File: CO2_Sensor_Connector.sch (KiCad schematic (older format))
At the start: 8 parts

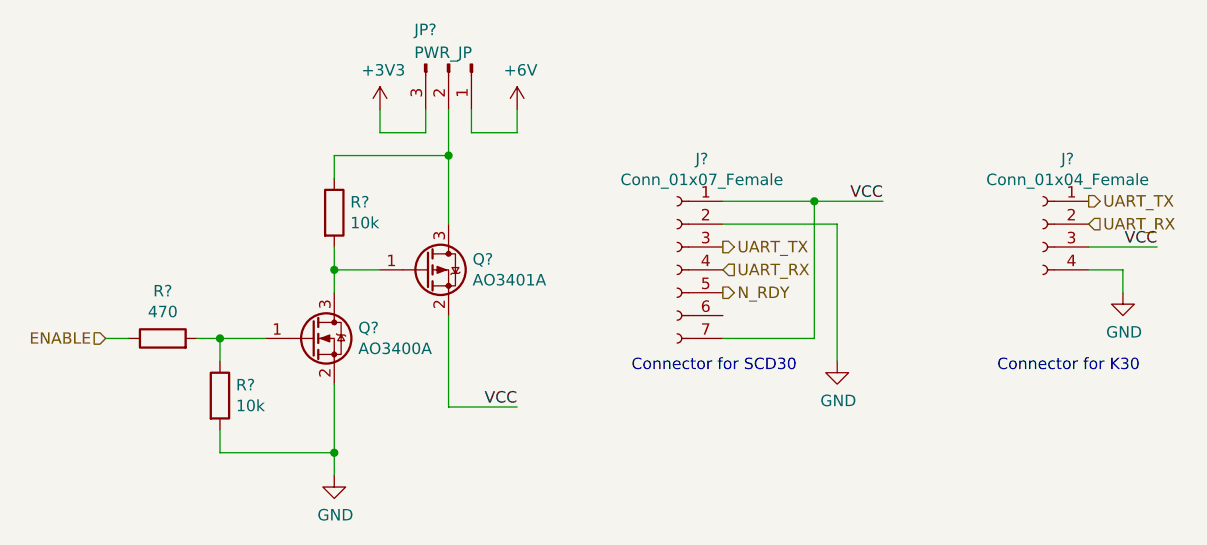
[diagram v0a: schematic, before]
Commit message: Change BME280 out for connector
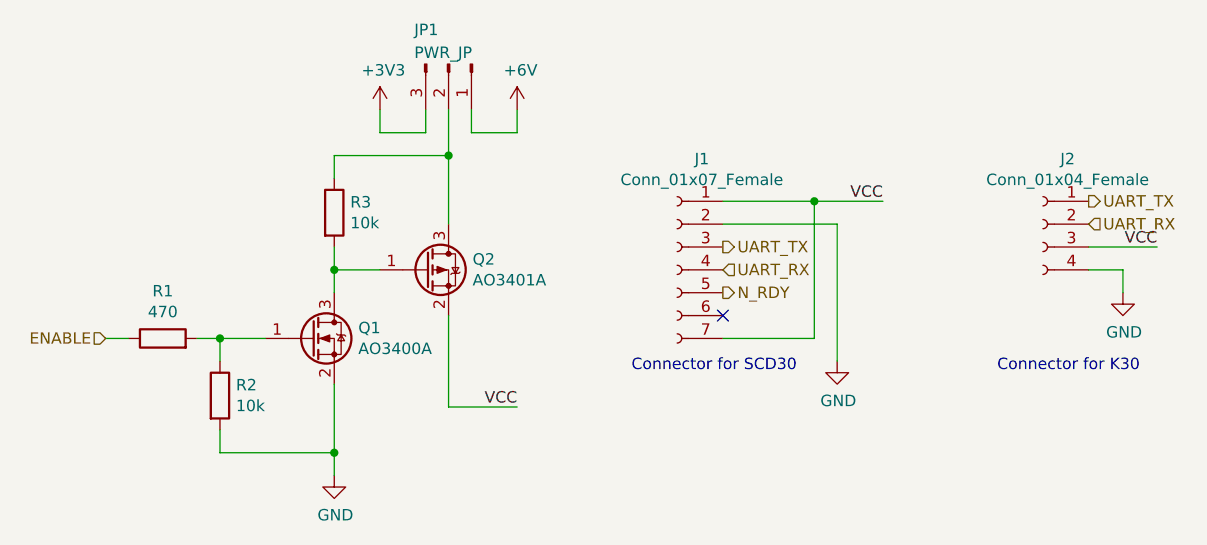
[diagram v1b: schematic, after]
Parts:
- gave numbers to parts that had none: 8
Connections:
- no-connect marks 0 -> 1
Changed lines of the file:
@@
 $Descr A4 11693 8268
 encoding utf-8
-Sheet 3 9
+Sheet 2 9
 Title ""
 Date ""
@@
 N_RDY
 $Comp
-L Connector:Conn_01x07_Female J?
+L Connector:Conn_01x07_Female J1
 U 1 1 60A57B40
 P 5800 3900
-AR Path="/60A49A7C/60A57B40" Ref="J?"  Part="1"
-AR Path="/60A4AC4A/60A57B40" Ref="J?"  Part="1"
-F 0 "J?" H 5692 4385 50  0000 C CNN
+AR Path="/60A49A7C/60A57B40" Ref="J1"  Part="1"
+AR Path="/60A4AC4A/60A57B40" Ref="J3"  Part="1"
+F 0 "J1" H 5692 4385 50  0000 C CNN
 F 1 "Conn_01x07_Female" H 5692 4294 50  0000 C CNN
 F 2 "" H 5800 3900 50  0001 C CNN
@@
 	6400 3600 6000 3600
 $Comp
-L power:GND #PWR?
+L power:GND #PWR04
 U 1 1 60A5D6A7
 P 6500 4300
-AR Path="/60A49A7C/60A5D6A7" Ref="#PWR?"  Part="1"
-AR Path="/60A4AC4A/60A5D6A7" Ref="#PWR?"  Part="1"
-F 0 "#PWR?" H 6500 4050 50  0001 C CNN
+AR Path="/60A49A7C/60A5D6A7" Ref="#PWR04"  Part="1"
+AR Path="/60A4AC4A/60A5D6A7" Ref="#PWR09"  Part="1"
+F 0 "#PWR09" H 6500 4050 50  0001 C CNN
 F 1 "GND" H 6505 4127 50  0000 C CNN
 F 2 "" H 6500 4300 50  0001 C CNN
@@
 	6400 4200 6400 3600
 $Comp
-L Transistor_FET:AO3401A Q?
+L Transistor_FET:AO3401A Q2
 U 1 1 60A6C14D
 P 4700 3900
-AR Path="/60A49A7C/60A6C14D" Ref="Q?"  Part="1"
-AR Path="/60A4AC4A/60A6C14D" Ref="Q?"  Part="1"
-F 0 "Q?" H 4905 3946 50  0000 L CNN
+AR Path="/60A49A7C/60A6C14D" Ref="Q2"  Part="1"
+AR Path="/60A4AC4A/60A6C14D" Ref="Q4"  Part="1"
+F 0 "Q2" H 4905 3946 50  0000 L CNN
 F 1 "AO3401A" H 4905 3855 50  0000 L CNN
 F 2 "Package_TO_SOT_SMD:SOT-23" H 4900 3825 50  0001 L CIN
@@
 $EndComp
 $Comp
-L Device:R R?
+L Device:R R1
 U 1 1 60A6FA21
 P 3550 4200
-AR Path="/60A49A7C/60A6FA21" Ref="R?"  Part="1"
-AR Path="/60A4AC4A/60A6FA21" Ref="R?"  Part="1"
-F 0 "R?" V 3757 4200 50  0000 C CNN
+AR Path="/60A49A7C/60A6FA21" Ref="R1"  Part="1"
+AR Path="/60A4AC4A/60A6FA21" Ref="R4"  Part="1"
+F 0 "R1" V 3757 4200 50  0000 C CNN
 F 1 "470" V 3666 4200 50  0000 C CNN
 F 2 "" V 3480 4200 50  0001 C CNN
@@
 	3400 4200 3300 4200
 $Comp
-L Device:R R?
+L Device:R R3
 U 1 1 60A736D3
 P 4300 3650
-AR Path="/60A49A7C/60A736D3" Ref="R?"  Part="1"
-AR Path="/60A4AC4A/60A736D3" Ref="R?"  Part="1"
-F 0 "R?" H 4370 3696 50  0000 L CNN
+AR Path="/60A49A7C/60A736D3" Ref="R3"  Part="1"
+AR Path="/60A4AC4A/60A736D3" Ref="R6"  Part="1"
+F 0 "R3" H 4370 3696 50  0000 L CNN
 F 1 "10k" H 4370 3605 50  0000 L CNN
 F 2 "" V 4230 3650 50  0001 C CNN
@@
 	4300 3500 4300 3400
 $Comp
-L Connector:Conn_01x03_Male JP?
+L Connector:Conn_01x03_Male JP1
 U 1 1 60A91C0B
 P 4800 3000
-AR Path="/60A49A7C/60A91C0B" Ref="JP?"  Part="1"
-AR Path="/60A4AC4A/60A91C0B" Ref="JP?"  Part="1"
-F 0 "JP?" V 4650 2850 50  0000 L CNN
+AR Path="/60A49A7C/60A91C0B" Ref="JP1"  Part="1"
+AR Path="/60A4AC4A/60A91C0B" Ref="JP2"  Part="1"
+F 0 "JP1" V 4650 2850 50  0000 L CNN
 F 1 "PWR_JP" V 4750 2850 50  0000 L CNN
 F 2 "" H 4800 3000 50  0001 C CNN
@@
 	4700 3200 4700 3300
 $Comp
-L power:+3V3 #PWR?
+L power:+3V3 #PWR02
 U 1 1 60A94D4D
 P 4500 3200
-AR Path="/60A49A7C/60A94D4D" Ref="#PWR?"  Part="1"
-AR Path="/60A4AC4A/60A94D4D" Ref="#PWR?"  Part="1"
-F 0 "#PWR?" H 4500 3050 50  0001 C CNN
+AR Path="/60A49A7C/60A94D4D" Ref="#PWR02"  Part="1"
+AR Path="/60A4AC4A/60A94D4D" Ref="#PWR07"  Part="1"
+F 0 "#PWR07" H 4500 3050 50  0001 C CNN
 F 1 "+3V3" H 4515 3373 50  0000 C CNN
 F 2 "" H 4500 3200 50  0001 C CNN
@@
 $EndComp
 $Comp
-L power:+6V #PWR?
+L power:+6V #PWR08
 U 1 1 60A9539A
 P 5100 3200
-AR Path="/60A49A7C/60A9539A" Ref="#PWR?"  Part="1"
-AR Path="/60A4AC4A/60A9539A" Ref="#PWR?"  Part="1"
-F 0 "#PWR?" H 5100 3050 50  0001 C CNN
+AR Path="/60A49A7C/60A9539A" Ref="#PWR08"  Part="1"
+AR Path="/60A4AC4A/60A9539A" Ref="#PWR0101"  Part="1"
+F 0 "#PWR0101" H 5100 3050 50  0001 C CNN
 F 1 "+6V" H 5115 3373 50  0000 C CNN
 F 2 "" H 5100 3200 50  0001 C CNN
@@
 	4900 3300 5100 3300
 $Comp
-L power:GND #PWR?
+L power:GND #PWR01
 U 1 1 60A9EA13
 P 4300 4800
-AR Path="/60A49A7C/60A9EA13" Ref="#PWR?"  Part="1"
-AR Path="/60A4AC4A/60A9EA13" Ref="#PWR?"  Part="1"
-F 0 "#PWR?" H 4300 4550 50  0001 C CNN
+AR Path="/60A49A7C/60A9EA13" Ref="#PWR01"  Part="1"
+AR Path="/60A4AC4A/60A9EA13" Ref="#PWR06"  Part="1"
+F 0 "#PWR06" H 4300 4550 50  0001 C CNN
 F 1 "GND" H 4305 4627 50  0000 C CNN
 F 2 "" H 4300 4800 50  0001 C CNN
@@
 VCC
 $Comp
-L Device:R R?
+L Device:R R2
 U 1 1 60AA508F
 P 3800 4450
-AR Path="/60A49A7C/60AA508F" Ref="R?"  Part="1"
-AR Path="/60A4AC4A/60AA508F" Ref="R?"  Part="1"
-F 0 "R?" H 3870 4496 50  0000 L CNN
+AR Path="/60A49A7C/60AA508F" Ref="R2"  Part="1"
+AR Path="/60A4AC4A/60AA508F" Ref="R5"  Part="1"
+F 0 "R2" H 3870 4496 50  0000 L CNN
 F 1 "10k" H 3870 4405 50  0000 L CNN
 F 2 "" V 3730 4450 50  0001 C CNN
@@
 	7600 3900 7750 3900
 $Comp
-L power:GND #PWR?
+L power:GND #PWR05
 U 1 1 60ABDE86
 P 7750 4000
-AR Path="/60A49A7C/60ABDE86" Ref="#PWR?"  Part="1"
-AR Path="/60A4AC4A/60ABDE86" Ref="#PWR?"  Part="1"
-F 0 "#PWR?" H 7750 3750 50  0001 C CNN
+AR Path="/60A49A7C/60ABDE86" Ref="#PWR05"  Part="1"
+AR Path="/60A4AC4A/60ABDE86" Ref="#PWR010"  Part="1"
+F 0 "#PWR010" H 7750 3750 50  0001 C CNN
 F 1 "GND" H 7755 3827 50  0000 C CNN
 F 2 "" H 7750 4000 50  0001 C CNN
@@
 $EndComp
 $Comp
-L Connector:Conn_01x04_Female J?
+L Connector:Conn_01x04_Female J2
 U 1 1 60ABE2B1
 P 7400 3700
-AR Path="/60A49A7C/60ABE2B1" Ref="J?"  Part="1"
-AR Path="/60A4AC4A/60ABE2B1" Ref="J?"  Part="1"
-F 0 "J?" H 7292 3985 50  0000 C CNN
+AR Path="/60A49A7C/60ABE2B1" Ref="J2"  Part="1"
+AR Path="/60A4AC4A/60ABE2B1" Ref="J4"  Part="1"
+F 0 "J2" H 7292 3985 50  0000 C CNN
 F 1 "Conn_01x04_Female" H 7292 3894 50  0000 C CNN
 F 2 "" H 7400 3700 50  0001 C CNN
@@
 	4800 4500 5100 4500
 $Comp
-L Transistor_FET:AO3400A Q?
+L Transistor_FET:AO3400A Q1
 U 1 1 60B57C20
 P 4200 4200
-AR Path="/60A49A7C/60B57C20" Ref="Q?"  Part="1"
-AR Path="/60A4AC4A/60B57C20" Ref="Q?"  Part="1"
-F 0 "Q?" H 4405 4246 50  0000 L CNN
+AR Path="/60A49A7C/60B57C20" Ref="Q1"  Part="1"
+AR Path="/60A4AC4A/60B57C20" Ref="Q3"  Part="1"
+F 0 "Q1" H 4405 4246 50  0000 L CNN
 F 1 "AO3400A" H 4405 4155 50  0000 L CNN
 F 2 "Package_TO_SOT_SMD:SOT-23" H 4400 4125 50  0001 L CIN
@@
 Wire Wire Line
 	3800 4200 4000 4200
+NoConn ~ 6000 4100
 $EndSCHEMATC

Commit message: Begin assigning footprints
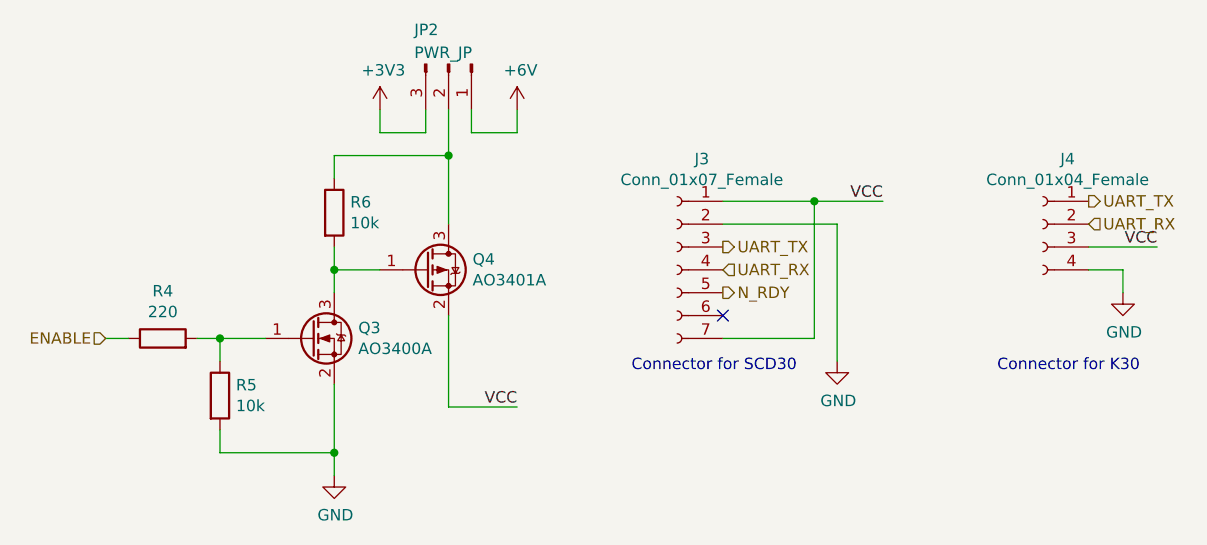
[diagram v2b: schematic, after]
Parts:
- J1: footprint (none) -> Connector_PinSocket_2.54mm:PinSocket_1x07_P2.54mm_Vertical
- J2: footprint (none) -> Connector_PinSocket_2.54mm:PinSocket_1x04_P2.54mm_Vertical
- JP1: footprint (none) -> Connector_PinHeader_2.54mm:PinHeader_1x03_P2.54mm_Vertical
- Q1: LCSC (none) -> C20917
- Q2: LCSC (none) -> C15127
- R1: value 470 -> 220; footprint (none) -> Resistor_SMD:R_0603_1608Metric; LCSC (none) -> C22962
- R2, R3: footprint (none) -> Resistor_SMD:R_0603_1608Metric; LCSC (none) -> C25804
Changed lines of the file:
@@
 AR Path="/60A49A7C/60A57B40" Ref="J1"  Part="1"
 AR Path="/60A4AC4A/60A57B40" Ref="J3"  Part="1"
-F 0 "J1" H 5692 4385 50  0000 C CNN
+F 0 "J3" H 5692 4385 50  0000 C CNN
 F 1 "Conn_01x07_Female" H 5692 4294 50  0000 C CNN
-F 2 "" H 5800 3900 50  0001 C CNN
+F 2 "Connector_PinSocket_2.54mm:PinSocket_1x07_P2.54mm_Vertical" H 5800 3900 50  0001 C CNN
 F 3 "~" H 5800 3900 50  0001 C CNN
 	1    5800 3900
@@
 AR Path="/60A49A7C/60A5D6A7" Ref="#PWR04"  Part="1"
 AR Path="/60A4AC4A/60A5D6A7" Ref="#PWR09"  Part="1"
-F 0 "#PWR09" H 6500 4050 50  0001 C CNN
+F 0 "#PWR04" H 6500 4050 50  0001 C CNN
 F 1 "GND" H 6505 4127 50  0000 C CNN
 F 2 "" H 6500 4300 50  0001 C CNN
@@
 AR Path="/60A49A7C/60A6C14D" Ref="Q2"  Part="1"
 AR Path="/60A4AC4A/60A6C14D" Ref="Q4"  Part="1"
-F 0 "Q2" H 4905 3946 50  0000 L CNN
+F 0 "Q4" H 4905 3946 50  0000 L CNN
 F 1 "AO3401A" H 4905 3855 50  0000 L CNN
 F 2 "Package_TO_SOT_SMD:SOT-23" H 4900 3825 50  0001 L CIN
 F 3 "http://www.aosmd.com/pdfs/datasheet/AO3401A.pdf" H 4700 3900 50  0001 L CNN
+F 4 "C15127" H 4700 3900 50  0001 C CNN "LCSC"
 	1    4700 3900
 	1    0    0    -1
@@
 AR Path="/60A49A7C/60A6FA21" Ref="R1"  Part="1"
 AR Path="/60A4AC4A/60A6FA21" Ref="R4"  Part="1"
-F 0 "R1" V 3757 4200 50  0000 C CNN
-F 1 "470" V 3666 4200 50  0000 C CNN
-F 2 "" V 3480 4200 50  0001 C CNN
+F 0 "R4" V 3757 4200 50  0000 C CNN
+F 1 "220" V 3666 4200 50  0000 C CNN
+F 2 "Resistor_SMD:R_0603_1608Metric" V 3480 4200 50  0001 C CNN
 F 3 "~" H 3550 4200 50  0001 C CNN
+F 4 "C22962" H 3550 4200 50  0001 C CNN "LCSC"
 	1    3550 4200
 	0    -1   -1   0
@@
 AR Path="/60A49A7C/60A736D3" Ref="R3"  Part="1"
 AR Path="/60A4AC4A/60A736D3" Ref="R6"  Part="1"
-F 0 "R3" H 4370 3696 50  0000 L CNN
+F 0 "R6" H 4370 3696 50  0000 L CNN
 F 1 "10k" H 4370 3605 50  0000 L CNN
-F 2 "" V 4230 3650 50  0001 C CNN
+F 2 "Resistor_SMD:R_0603_1608Metric" V 4230 3650 50  0001 C CNN
 F 3 "~" H 4300 3650 50  0001 C CNN
+F 4 "C25804" H 4300 3650 50  0001 C CNN "LCSC"
 	1    4300 3650
 	1    0    0    -1
@@
 AR Path="/60A49A7C/60A91C0B" Ref="JP1"  Part="1"
 AR Path="/60A4AC4A/60A91C0B" Ref="JP2"  Part="1"
-F 0 "JP1" V 4650 2850 50  0000 L CNN
+F 0 "JP2" V 4650 2850 50  0000 L CNN
 F 1 "PWR_JP" V 4750 2850 50  0000 L CNN
-F 2 "" H 4800 3000 50  0001 C CNN
+F 2 "Connector_PinHeader_2.54mm:PinHeader_1x03_P2.54mm_Vertical" H 4800 3000 50  0001 C CNN
 F 3 "~" H 4800 3000 50  0001 C CNN
 	1    4800 3000
@@
 AR Path="/60A49A7C/60A94D4D" Ref="#PWR02"  Part="1"
 AR Path="/60A4AC4A/60A94D4D" Ref="#PWR07"  Part="1"
-F 0 "#PWR07" H 4500 3050 50  0001 C CNN
+F 0 "#PWR02" H 4500 3050 50  0001 C CNN
 F 1 "+3V3" H 4515 3373 50  0000 C CNN
 F 2 "" H 4500 3200 50  0001 C CNN
@@
 $EndComp
 $Comp
-L power:+6V #PWR08
+L power:+6V #PWR03
 U 1 1 60A9539A
 P 5100 3200
-AR Path="/60A49A7C/60A9539A" Ref="#PWR08"  Part="1"
-AR Path="/60A4AC4A/60A9539A" Ref="#PWR0101"  Part="1"
-F 0 "#PWR0101" H 5100 3050 50  0001 C CNN
+AR Path="/60A49A7C/60A9539A" Ref="#PWR03"  Part="1"
+AR Path="/60A4AC4A/60A9539A" Ref="#PWR08"  Part="1"
+F 0 "#PWR03" H 5100 3050 50  0001 C CNN
 F 1 "+6V" H 5115 3373 50  0000 C CNN
 F 2 "" H 5100 3200 50  0001 C CNN
@@
 AR Path="/60A49A7C/60A9EA13" Ref="#PWR01"  Part="1"
 AR Path="/60A4AC4A/60A9EA13" Ref="#PWR06"  Part="1"
-F 0 "#PWR06" H 4300 4550 50  0001 C CNN
+F 0 "#PWR01" H 4300 4550 50  0001 C CNN
 F 1 "GND" H 4305 4627 50  0000 C CNN
 F 2 "" H 4300 4800 50  0001 C CNN
@@
 AR Path="/60A49A7C/60AA508F" Ref="R2"  Part="1"
 AR Path="/60A4AC4A/60AA508F" Ref="R5"  Part="1"
-F 0 "R2" H 3870 4496 50  0000 L CNN
+F 0 "R5" H 3870 4496 50  0000 L CNN
 F 1 "10k" H 3870 4405 50  0000 L CNN
-F 2 "" V 3730 4450 50  0001 C CNN
+F 2 "Resistor_SMD:R_0603_1608Metric" V 3730 4450 50  0001 C CNN
 F 3 "~" H 3800 4450 50  0001 C CNN
+F 4 "C25804" H 3800 4450 50  0001 C CNN "LCSC"
 	1    3800 4450
 	1    0    0    -1
@@
 AR Path="/60A49A7C/60ABDE86" Ref="#PWR05"  Part="1"
 AR Path="/60A4AC4A/60ABDE86" Ref="#PWR010"  Part="1"
-F 0 "#PWR010" H 7750 3750 50  0001 C CNN
+F 0 "#PWR05" H 7750 3750 50  0001 C CNN
 F 1 "GND" H 7755 3827 50  0000 C CNN
 F 2 "" H 7750 4000 50  0001 C CNN
@@
 AR Path="/60A49A7C/60ABE2B1" Ref="J2"  Part="1"
 AR Path="/60A4AC4A/60ABE2B1" Ref="J4"  Part="1"
-F 0 "J2" H 7292 3985 50  0000 C CNN
+F 0 "J4" H 7292 3985 50  0000 C CNN
 F 1 "Conn_01x04_Female" H 7292 3894 50  0000 C CNN
-F 2 "" H 7400 3700 50  0001 C CNN
+F 2 "Connector_PinSocket_2.54mm:PinSocket_1x04_P2.54mm_Vertical" H 7400 3700 50  0001 C CNN
 F 3 "~" H 7400 3700 50  0001 C CNN
 	1    7400 3700
@@
 AR Path="/60A49A7C/60B57C20" Ref="Q1"  Part="1"
 AR Path="/60A4AC4A/60B57C20" Ref="Q3"  Part="1"
-F 0 "Q1" H 4405 4246 50  0000 L CNN
+F 0 "Q3" H 4405 4246 50  0000 L CNN
 F 1 "AO3400A" H 4405 4155 50  0000 L CNN
 F 2 "Package_TO_SOT_SMD:SOT-23" H 4400 4125 50  0001 L CIN
 F 3 "http://www.aosmd.com/pdfs/datasheet/AO3400A.pdf" H 4200 4200 50  0001 L CNN
+F 4 "C20917" H 4200 4200 50  0001 C CNN "LCSC"
 	1    4200 4200
 	1    0    0    -1

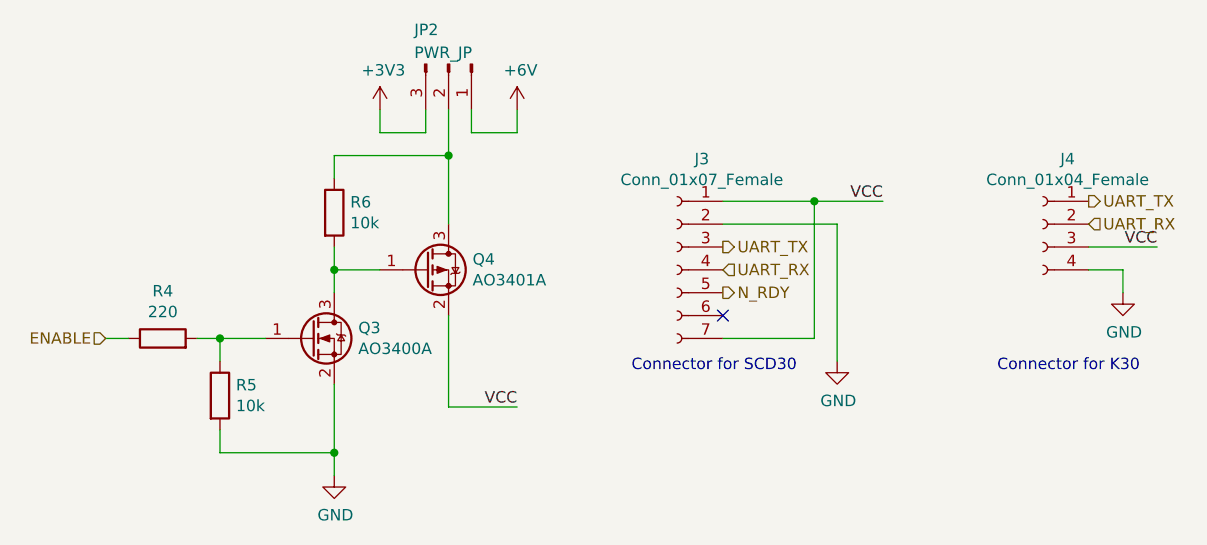
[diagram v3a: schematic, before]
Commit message: Start changing buck converters
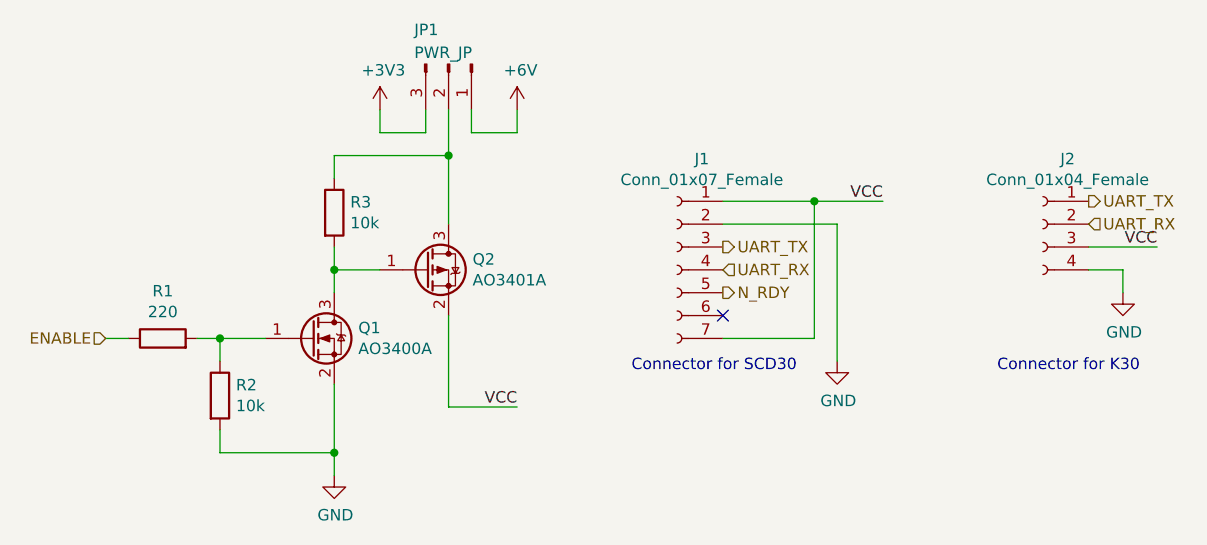
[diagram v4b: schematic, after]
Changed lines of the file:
@@
 AR Path="/60A49A7C/60A57B40" Ref="J1"  Part="1"
 AR Path="/60A4AC4A/60A57B40" Ref="J3"  Part="1"
-F 0 "J3" H 5692 4385 50  0000 C CNN
+F 0 "J1" H 5692 4385 50  0000 C CNN
 F 1 "Conn_01x07_Female" H 5692 4294 50  0000 C CNN
 F 2 "Connector_PinSocket_2.54mm:PinSocket_1x07_P2.54mm_Vertical" H 5800 3900 50  0001 C CNN
@@
 AR Path="/60A49A7C/60A5D6A7" Ref="#PWR04"  Part="1"
 AR Path="/60A4AC4A/60A5D6A7" Ref="#PWR09"  Part="1"
-F 0 "#PWR09" H 6500 4050 50  0001 C CNN
+F 0 "#PWR04" H 6500 4050 50  0001 C CNN
 F 1 "GND" H 6505 4127 50  0000 C CNN
 F 2 "" H 6500 4300 50  0001 C CNN
@@
 AR Path="/60A49A7C/60A6C14D" Ref="Q2"  Part="1"
 AR Path="/60A4AC4A/60A6C14D" Ref="Q4"  Part="1"
-F 0 "Q4" H 4905 3946 50  0000 L CNN
+F 0 "Q2" H 4905 3946 50  0000 L CNN
 F 1 "AO3401A" H 4905 3855 50  0000 L CNN
 F 2 "Package_TO_SOT_SMD:SOT-23" H 4900 3825 50  0001 L CIN
@@
 AR Path="/60A49A7C/60A6FA21" Ref="R1"  Part="1"
 AR Path="/60A4AC4A/60A6FA21" Ref="R4"  Part="1"
-F 0 "R4" V 3757 4200 50  0000 C CNN
+F 0 "R1" V 3757 4200 50  0000 C CNN
 F 1 "220" V 3666 4200 50  0000 C CNN
 F 2 "Resistor_SMD:R_0603_1608Metric" V 3480 4200 50  0001 C CNN
@@
 AR Path="/60A49A7C/60A736D3" Ref="R3"  Part="1"
 AR Path="/60A4AC4A/60A736D3" Ref="R6"  Part="1"
-F 0 "R6" H 4370 3696 50  0000 L CNN
+F 0 "R3" H 4370 3696 50  0000 L CNN
 F 1 "10k" H 4370 3605 50  0000 L CNN
 F 2 "Resistor_SMD:R_0603_1608Metric" V 4230 3650 50  0001 C CNN
@@
 AR Path="/60A49A7C/60A91C0B" Ref="JP1"  Part="1"
 AR Path="/60A4AC4A/60A91C0B" Ref="JP2"  Part="1"
-F 0 "JP2" V 4650 2850 50  0000 L CNN
+F 0 "JP1" V 4650 2850 50  0000 L CNN
 F 1 "PWR_JP" V 4750 2850 50  0000 L CNN
 F 2 "Connector_PinHeader_2.54mm:PinHeader_1x03_P2.54mm_Vertical" H 4800 3000 50  0001 C CNN
@@
 AR Path="/60A49A7C/60A94D4D" Ref="#PWR02"  Part="1"
 AR Path="/60A4AC4A/60A94D4D" Ref="#PWR07"  Part="1"
-F 0 "#PWR07" H 4500 3050 50  0001 C CNN
+F 0 "#PWR02" H 4500 3050 50  0001 C CNN
 F 1 "+3V3" H 4515 3373 50  0000 C CNN
 F 2 "" H 4500 3200 50  0001 C CNN
@@
 AR Path="/60A49A7C/60A9539A" Ref="#PWR03"  Part="1"
 AR Path="/60A4AC4A/60A9539A" Ref="#PWR08"  Part="1"
-F 0 "#PWR08" H 5100 3050 50  0001 C CNN
+F 0 "#PWR03" H 5100 3050 50  0001 C CNN
 F 1 "+6V" H 5115 3373 50  0000 C CNN
 F 2 "" H 5100 3200 50  0001 C CNN
@@
 AR Path="/60A49A7C/60A9EA13" Ref="#PWR01"  Part="1"
 AR Path="/60A4AC4A/60A9EA13" Ref="#PWR06"  Part="1"
-F 0 "#PWR06" H 4300 4550 50  0001 C CNN
+F 0 "#PWR01" H 4300 4550 50  0001 C CNN
 F 1 "GND" H 4305 4627 50  0000 C CNN
 F 2 "" H 4300 4800 50  0001 C CNN
@@
 AR Path="/60A49A7C/60AA508F" Ref="R2"  Part="1"
 AR Path="/60A4AC4A/60AA508F" Ref="R5"  Part="1"
-F 0 "R5" H 3870 4496 50  0000 L CNN
+F 0 "R2" H 3870 4496 50  0000 L CNN
 F 1 "10k" H 3870 4405 50  0000 L CNN
 F 2 "Resistor_SMD:R_0603_1608Metric" V 3730 4450 50  0001 C CNN
@@
 AR Path="/60A49A7C/60ABDE86" Ref="#PWR05"  Part="1"
 AR Path="/60A4AC4A/60ABDE86" Ref="#PWR010"  Part="1"
-F 0 "#PWR010" H 7750 3750 50  0001 C CNN
+F 0 "#PWR05" H 7750 3750 50  0001 C CNN
 F 1 "GND" H 7755 3827 50  0000 C CNN
 F 2 "" H 7750 4000 50  0001 C CNN
@@
 AR Path="/60A49A7C/60ABE2B1" Ref="J2"  Part="1"
 AR Path="/60A4AC4A/60ABE2B1" Ref="J4"  Part="1"
-F 0 "J4" H 7292 3985 50  0000 C CNN
+F 0 "J2" H 7292 3985 50  0000 C CNN
 F 1 "Conn_01x04_Female" H 7292 3894 50  0000 C CNN
 F 2 "Connector_PinSocket_2.54mm:PinSocket_1x04_P2.54mm_Vertical" H 7400 3700 50  0001 C CNN
@@
 AR Path="/60A49A7C/60B57C20" Ref="Q1"  Part="1"
 AR Path="/60A4AC4A/60B57C20" Ref="Q3"  Part="1"
-F 0 "Q3" H 4405 4246 50  0000 L CNN
+F 0 "Q1" H 4405 4246 50  0000 L CNN
 F 1 "AO3400A" H 4405 4155 50  0000 L CNN
 F 2 "Package_TO_SOT_SMD:SOT-23" H 4400 4125 50  0001 L CIN

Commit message: Export fabrication files
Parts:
- J1: LCSC (none) -> C358721
- JP1: LCSC (none) -> C306138
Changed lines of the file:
@@
 F 2 "Connector_PinSocket_2.54mm:PinSocket_1x07_P2.54mm_Vertical" H 5800 3900 50  0001 C CNN
 F 3 "~" H 5800 3900 50  0001 C CNN
+F 4 "C358721" H 5800 3900 50  0001 C CNN "LCSC"
 	1    5800 3900
 	-1   0    0    -1
@@
 F 2 "Connector_PinHeader_2.54mm:PinHeader_1x03_P2.54mm_Vertical" H 4800 3000 50  0001 C CNN
 F 3 "~" H 4800 3000 50  0001 C CNN
+F 4 "C306138" H 4800 3000 50  0001 C CNN "LCSC"
 	1    4800 3000
 	0    1    1    0
